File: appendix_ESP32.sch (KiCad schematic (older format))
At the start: 1 part

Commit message: pre Annotation 1
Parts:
- added Q? (x2): 2N3904, digikey-footprints:TO-92-3, symbol dk_Transistors-Bipolar-BJT-Single:2N3904
- added R? (x3): 10k, symbol Device:R
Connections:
- net labels added: DTR_ESP32, ESP32_GPIO0, ESP32_RESET, RTS_ESP32
- wire segments 4 -> 24
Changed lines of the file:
@@
 $Descr A4 11693 8268
 encoding utf-8
-Sheet 3 7
+Sheet 3 6
 Title ""
 Date ""
@@
 EndData
 $EndBitmap
+$Comp
+L dk_Transistors-Bipolar-BJT-Single:2N3904 Q?
+U 1 1 5CBEF82D
+P 9500 2350
+F 0 "Q?" H 9688 2403 60  0000 L CNN
+F 1 "2N3904" H 9688 2297 60  0000 L CNN
+F 2 "digikey-footprints:TO-92-3" H 9700 2550 60  0001 L CNN
+F 3 "https://my.centralsemi.com/get_document.php?cmp=1&mergetype=pd&mergepath=pd&pdf_id=LSSGP072.PDF" H 9700 2650 60  0001 L CNN
+F 4 "2N3904CS-ND" H 9700 2750 60  0001 L CNN "Digi-Key_PN"
+F 5 "2N3904" H 9700 2850 60  0001 L CNN "MPN"
+F 6 "Discrete Semiconductor Products" H 9700 2950 60  0001 L CNN "Category"
+F 7 "Transistors - Bipolar (BJT) - Single" H 9700 3050 60  0001 L CNN "Family"
+F 8 "https://my.centralsemi.com/get_document.php?cmp=1&mergetype=pd&mergepath=pd&pdf_id=LSSGP072.PDF" H 9700 3150 60  0001 L CNN "DK_Datasheet_Link"
+F 9 "/product-detail/en/central-semiconductor-corp/2N3904/2N3904CS-ND/4806876" H 9700 3250 60  0001 L CNN "DK_Detail_Page"
+F 10 "TRANS NPN 40V TO-92" H 9700 3350 60  0001 L CNN "Description"
+F 11 "Central Semiconductor Corp" H 9700 3450 60  0001 L CNN "Manufacturer"
+F 12 "Active" H 9700 3550 60  0001 L CNN "Status"
+	1    9500 2350
+	1    0    0    -1
+$EndComp
+$Comp
+L dk_Transistors-Bipolar-BJT-Single:2N3904 Q?
+U 1 1 5CBF1B4A
+P 9500 3000
+F 0 "Q?" H 9688 2947 60  0000 L CNN
+F 1 "2N3904" H 9688 3053 60  0000 L CNN
+F 2 "digikey-footprints:TO-92-3" H 9700 3200 60  0001 L CNN
+F 3 "https://my.centralsemi.com/get_document.php?cmp=1&mergetype=pd&mergepath=pd&pdf_id=LSSGP072.PDF" H 9700 3300 60  0001 L CNN
+F 4 "2N3904CS-ND" H 9700 3400 60  0001 L CNN "Digi-Key_PN"
+F 5 "2N3904" H 9700 3500 60  0001 L CNN "MPN"
+F 6 "Discrete Semiconductor Products" H 9700 3600 60  0001 L CNN "Category"
+F 7 "Transistors - Bipolar (BJT) - Single" H 9700 3700 60  0001 L CNN "Family"
+F 8 "https://my.centralsemi.com/get_document.php?cmp=1&mergetype=pd&mergepath=pd&pdf_id=LSSGP072.PDF" H 9700 3800 60  0001 L CNN "DK_Datasheet_Link"
+F 9 "/product-detail/en/central-semiconductor-corp/2N3904/2N3904CS-ND/4806876" H 9700 3900 60  0001 L CNN "DK_Detail_Page"
+F 10 "TRANS NPN 40V TO-92" H 9700 4000 60  0001 L CNN "Description"
+F 11 "Central Semiconductor Corp" H 9700 4100 60  0001 L CNN "Manufacturer"
+F 12 "Active" H 9700 4200 60  0001 L CNN "Status"
+	1    9500 3000
+	1    0    0    1
+$EndComp
+$Comp
+L Device:R R?
+U 1 1 5CBF31BB
+P 9000 2350
+F 0 "R?" V 8793 2350 50  0000 C CNN
+F 1 "10k" V 8884 2350 50  0000 C CNN
+F 2 "" V 8930 2350 50  0001 C CNN
+F 3 "~" H 9000 2350 50  0001 C CNN
+	1    9000 2350
+	0    1    1    0
+$EndComp
+$Comp
+L Device:R R?
+U 1 1 5CBF3EA7
+P 9000 3000
+F 0 "R?" V 8793 3000 50  0000 C CNN
+F 1 "10k" V 8884 3000 50  0000 C CNN
+F 2 "" V 8930 3000 50  0001 C CNN
+F 3 "~" H 9000 3000 50  0001 C CNN
+	1    9000 3000
+	0    1    1    0
+$EndComp
+Wire Wire Line
+	9150 3000 9300 3000
+Wire Wire Line
+	9150 2350 9300 2350
+Wire Wire Line
+	8850 3000 8650 3000
+Wire Wire Line
+	9600 2550 9400 2750
+Wire Wire Line
+	8650 2750 9400 2750
+Wire Wire Line
+	8850 2350 8650 2350
+Wire Wire Line
+	8650 2350 8650 2600
+Wire Wire Line
+	8650 2600 9400 2600
+Wire Wire Line
+	9400 2600 9600 2800
+Wire Wire Line
+	8650 2750 8650 3000
+Wire Wire Line
+	8650 2350 8350 2350
+Connection ~ 8650 2350
+Wire Wire Line
+	8650 3000 8350 3000
+Connection ~ 8650 3000
+Text HLabel 8350 3000 0    50   Input ~ 0
+DTR_ESP32
+Text HLabel 8350 2350 0    50   Input ~ 0
+RTS_ESP32
+Wire Wire Line
+	5650 2100 5850 2100
+Text Label 5850 2100 0    50   ~ 0
+ESP32_GPIO0
+Text Label 9650 2100 0    50   ~ 0
+ESP32_GPIO0
+Text Label 9650 3250 0    50   ~ 0
+ESP32_RESET
+Wire Wire Line
+	9650 3250 9600 3250
+Wire Wire Line
+	9600 3250 9600 3200
+Wire Wire Line
+	9600 2150 9600 2100
+Wire Wire Line
+	9600 2100 9650 2100
+Text Label 3550 2100 0    50   ~ 0
+ESP32_RESET
+$Comp
+L Device:R R?
+U 1 1 5CBFAC95
+P 4200 1900
+F 0 "R?" H 4270 1946 50  0000 L CNN
+F 1 "10k" H 4270 1855 50  0000 L CNN
+F 2 "" V 4130 1900 50  0001 C CNN
+F 3 "~" H 4200 1900 50  0001 C CNN
+	1    4200 1900
+	1    0    0    -1
+$EndComp
+$Comp
+L power:+3.3V #PWR?
+U 1 1 5CBFC50E
+P 4200 1750
+F 0 "#PWR?" H 4200 1600 50  0001 C CNN
+F 1 "+3.3V" H 4215 1923 50  0000 C CNN
+F 2 "" H 4200 1750 50  0001 C CNN
+F 3 "" H 4200 1750 50  0001 C CNN
+	1    4200 1750
+	1    0    0    -1
+$EndComp
+Wire Wire Line
+	4450 2100 4200 2100
+Wire Wire Line
+	4200 2050 4200 2100
+Connection ~ 4200 2100
+Wire Wire Line
+	4200 2100 3550 2100
 $EndSCHEMATC

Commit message: 1st annotation, footprints, netlist
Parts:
- R301, R302, R303: renamed from R?; footprint (none) -> Resistors_SMD:R_0805
- gave numbers to parts that had none: 3
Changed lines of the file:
@@
 $EndDescr
 $Comp
-L power:GND #PWR?
+L power:GND #PWR0136
 U 1 1 5CA3C9F2
 P 5050 4850
-F 0 "#PWR?" H 5050 4600 50  0001 C CNN
+F 0 "#PWR0136" H 5050 4600 50  0001 C CNN
 F 1 "GND" H 5055 4677 50  0000 C CNN
 F 2 "" H 5050 4850 50  0001 C CNN
@@
 $EndComp
 $Comp
-L power:+3.3V #PWR?
+L power:+3.3V #PWR0137
 U 1 1 5CA3CA30
 P 5050 1750
-F 0 "#PWR?" H 5050 1600 50  0001 C CNN
+F 0 "#PWR0137" H 5050 1600 50  0001 C CNN
 F 1 "+3.3V" H 5065 1923 50  0000 C CNN
 F 2 "" H 5050 1750 50  0001 C CNN
@@
 D_RX_to_ESP_TX
 $Comp
-L RF_Module:ESP32-WROOM-32 U?
+L RF_Module:ESP32-WROOM-32 U301
 U 1 1 5CA47080
 P 5050 3300
-F 0 "U?" H 5300 4850 50  0000 C CNN
+F 0 "U301" H 5300 4850 50  0000 C CNN
 F 1 "ESP32-WROOM-32" H 5600 4750 50  0000 C CNN
 F 2 "RF_Module:ESP32-WROOM-32" H 5050 1800 50  0001 C CNN
@@
 $EndBitmap
 $Comp
-L dk_Transistors-Bipolar-BJT-Single:2N3904 Q?
+L dk_Transistors-Bipolar-BJT-Single:2N3904 Q301
 U 1 1 5CBEF82D
 P 9500 2350
-F 0 "Q?" H 9688 2403 60  0000 L CNN
+F 0 "Q301" H 9688 2403 60  0000 L CNN
 F 1 "2N3904" H 9688 2297 60  0000 L CNN
 F 2 "digikey-footprints:TO-92-3" H 9700 2550 60  0001 L CNN
@@
 $EndComp
 $Comp
-L dk_Transistors-Bipolar-BJT-Single:2N3904 Q?
+L dk_Transistors-Bipolar-BJT-Single:2N3904 Q302
 U 1 1 5CBF1B4A
 P 9500 3000
-F 0 "Q?" H 9688 2947 60  0000 L CNN
+F 0 "Q302" H 9688 2947 60  0000 L CNN
 F 1 "2N3904" H 9688 3053 60  0000 L CNN
 F 2 "digikey-footprints:TO-92-3" H 9700 3200 60  0001 L CNN
@@
 $EndComp
 $Comp
-L Device:R R?
+L Device:R R302
 U 1 1 5CBF31BB
 P 9000 2350
-F 0 "R?" V 8793 2350 50  0000 C CNN
+F 0 "R302" V 8793 2350 50  0000 C CNN
 F 1 "10k" V 8884 2350 50  0000 C CNN
-F 2 "" V 8930 2350 50  0001 C CNN
+F 2 "Resistors_SMD:R_0805" V 8930 2350 50  0001 C CNN
 F 3 "~" H 9000 2350 50  0001 C CNN
 	1    9000 2350
@@
 $EndComp
 $Comp
-L Device:R R?
+L Device:R R303
 U 1 1 5CBF3EA7
 P 9000 3000
-F 0 "R?" V 8793 3000 50  0000 C CNN
+F 0 "R303" V 8793 3000 50  0000 C CNN
 F 1 "10k" V 8884 3000 50  0000 C CNN
-F 2 "" V 8930 3000 50  0001 C CNN
+F 2 "Resistors_SMD:R_0805" V 8930 3000 50  0001 C CNN
 F 3 "~" H 9000 3000 50  0001 C CNN
 	1    9000 3000
@@
 ESP32_RESET
 $Comp
-L Device:R R?
+L Device:R R301
 U 1 1 5CBFAC95
 P 4200 1900
-F 0 "R?" H 4270 1946 50  0000 L CNN
+F 0 "R301" H 4270 1946 50  0000 L CNN
 F 1 "10k" H 4270 1855 50  0000 L CNN
-F 2 "" V 4130 1900 50  0001 C CNN
+F 2 "Resistors_SMD:R_0805" V 4130 1900 50  0001 C CNN
 F 3 "~" H 4200 1900 50  0001 C CNN
 	1    4200 1900
@@
 $EndComp
 $Comp
-L power:+3.3V #PWR?
+L power:+3.3V #PWR0138
 U 1 1 5CBFC50E
 P 4200 1750
-F 0 "#PWR?" H 4200 1600 50  0001 C CNN
+F 0 "#PWR0138" H 4200 1600 50  0001 C CNN
 F 1 "+3.3V" H 4215 1923 50  0000 C CNN
 F 2 "" H 4200 1750 50  0001 C CNN

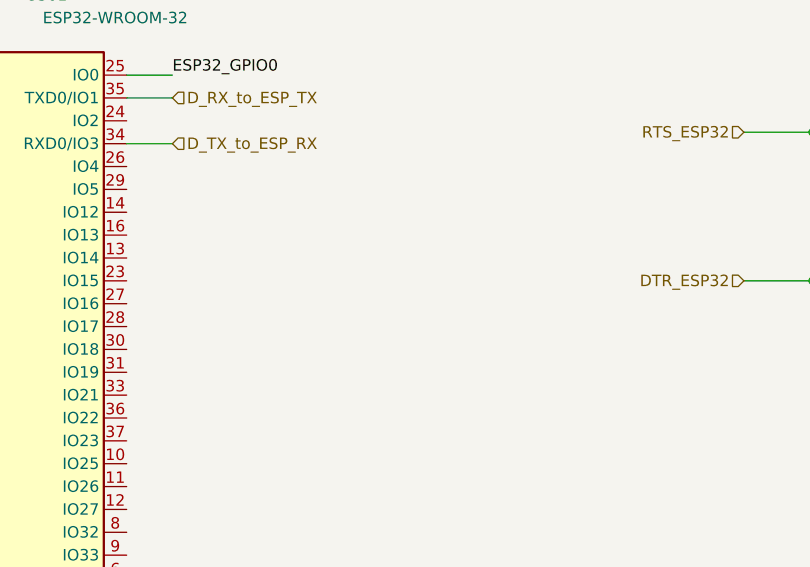
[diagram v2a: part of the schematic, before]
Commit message: started layouting TMC2660
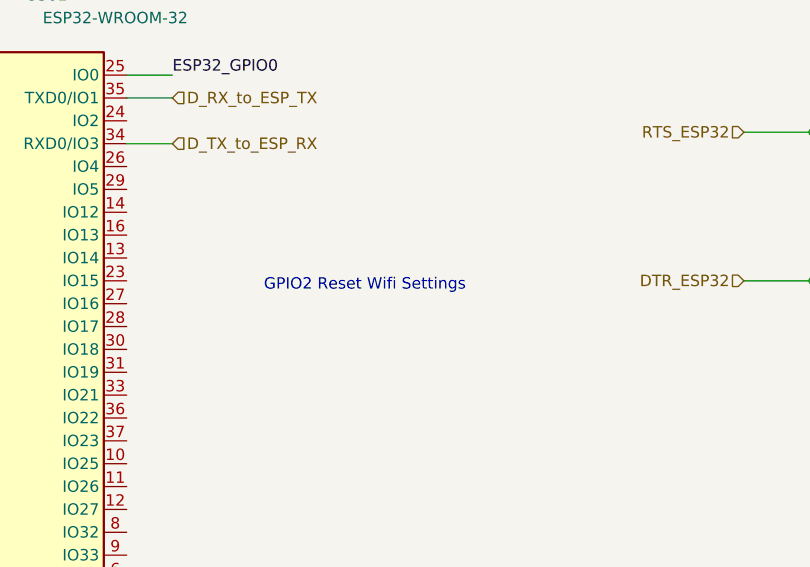
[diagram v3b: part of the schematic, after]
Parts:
- R301, R302, R303: footprint Resistors_SMD:R_0805 -> Resistors_SMD:R_0603
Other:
- note added: "GPIO2 Reset Wifi Settings"
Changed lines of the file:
@@
 F 0 "R302" V 8793 2350 50  0000 C CNN
 F 1 "10k" V 8884 2350 50  0000 C CNN
-F 2 "Resistors_SMD:R_0805" V 8930 2350 50  0001 C CNN
+F 2 "Resistors_SMD:R_0603" V 8930 2350 50  0001 C CNN
 F 3 "~" H 9000 2350 50  0001 C CNN
 	1    9000 2350
@@
 F 0 "R303" V 8793 3000 50  0000 C CNN
 F 1 "10k" V 8884 3000 50  0000 C CNN
-F 2 "Resistors_SMD:R_0805" V 8930 3000 50  0001 C CNN
+F 2 "Resistors_SMD:R_0603" V 8930 3000 50  0001 C CNN
 F 3 "~" H 9000 3000 50  0001 C CNN
 	1    9000 3000
@@
 F 0 "R301" H 4270 1946 50  0000 L CNN
 F 1 "10k" H 4270 1855 50  0000 L CNN
-F 2 "Resistors_SMD:R_0805" V 4130 1900 50  0001 C CNN
+F 2 "Resistors_SMD:R_0603" V 4130 1900 50  0001 C CNN
 F 3 "~" H 4200 1900 50  0001 C CNN
 	1    4200 1900
@@
 Wire Wire Line
 	4200 2100 3550 2100
+Text Notes 6250 3050 0    50   ~ 0
+GPIO2 Reset Wifi Settings
 $EndSCHEMATC

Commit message: Layout: all TMC / Schematic: Oli's comments
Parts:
- added C301, C302: 100n, Capacitors_SMD:C_0603, symbol Device:C
- added R304: 10k, Resistors_SMD:R_0603, symbol Device:R
- added SW301, SW302: SW_Push, Button_Switch_SMD:SW_Push_1P1T_NO_CK_KMR2, symbol Switch:SW_Push
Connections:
- wire segments 24 -> 41
- no-connect marks 0 -> 27
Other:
- note added: "ESP3D Settings Reset"
- note removed: "GPIO2 Reset Wifi Settings"
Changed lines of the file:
@@
 Connection ~ 4200 2100
 Wire Wire Line
-	4200 2100 3550 2100
-Text Notes 6250 3050 0    50   ~ 0
-GPIO2 Reset Wifi Settings
+	4200 2100 3900 2100
+Text Notes 6300 3750 0    50   ~ 0
+ESP3D Settings Reset
+$Comp
+L Switch:SW_Push SW?
+U 1 1 5CD80C30
+P 6500 4050
+AR Path="/5CA3954A/5CD80C30" Ref="SW?"  Part="1"
+AR Path="/5CA395A8/5CD80C30" Ref="SW302"  Part="1"
+F 0 "SW302" V 6650 4250 50  0000 C CNN
+F 1 "SW_Push" V 6300 4300 50  0000 C CNN
+F 2 "Button_Switch_SMD:SW_Push_1P1T_NO_CK_KMR2" H 6500 4250 50  0001 C CNN
+F 3 "~" H 6500 4250 50  0001 C CNN
+	1    6500 4050
+	0    1    -1   0
+$EndComp
+$Comp
+L Device:C C?
+U 1 1 5CD80C36
+P 6200 4050
+AR Path="/5CA3954A/5CD80C36" Ref="C?"  Part="1"
+AR Path="/5CA395A8/5CD80C36" Ref="C302"  Part="1"
+F 0 "C302" H 6000 4150 50  0000 C CNN
+F 1 "100n" H 6350 4150 50  0000 C CNN
+F 2 "Capacitors_SMD:C_0603" H 6238 3900 50  0001 C CNN
+F 3 "~" H 6200 4050 50  0001 C CNN
+	1    6200 4050
+	-1   0    0    -1
+$EndComp
+$Comp
+L power:GND #PWR?
+U 1 1 5CD80C3C
+P 6200 4400
+AR Path="/5CA3954A/5CD80C3C" Ref="#PWR?"  Part="1"
+AR Path="/5CA395A8/5CD80C3C" Ref="#PWR0303"  Part="1"
+F 0 "#PWR0303" H 6200 4150 50  0001 C CNN
+F 1 "GND" H 6205 4227 50  0000 C CNN
+F 2 "" H 6200 4400 50  0001 C CNN
+F 3 "" H 6200 4400 50  0001 C CNN
+	1    6200 4400
+	-1   0    0    -1
+$EndComp
+Wire Wire Line
+	6500 4250 6500 4300
+Wire Wire Line
+	6500 4300 6200 4300
+Wire Wire Line
+	6200 4300 6200 4200
+Wire Wire Line
+	6200 3900 6200 3800
+Wire Wire Line
+	6200 3800 6500 3800
+Wire Wire Line
+	6500 3800 6500 3850
+Wire Wire Line
+	6200 4400 6200 4300
+Connection ~ 6200 4300
+Connection ~ 6200 3800
+$Comp
+L Device:R R?
+U 1 1 5CD80C4C
+P 6200 3600
+AR Path="/5CA3954A/5CD80C4C" Ref="R?"  Part="1"
+AR Path="/5CA395A8/5CD80C4C" Ref="R304"  Part="1"
+F 0 "R304" H 6270 3646 50  0000 L CNN
+F 1 "10k" H 6270 3555 50  0000 L CNN
+F 2 "Resistors_SMD:R_0603" V 6130 3600 50  0001 C CNN
+F 3 "~" H 6200 3600 50  0001 C CNN
+	1    6200 3600
+	-1   0    0    -1
+$EndComp
+Wire Wire Line
+	6200 3800 6200 3750
+$Comp
+L power:+3.3V #PWR?
+U 1 1 5CD80C53
+P 6200 3400
+AR Path="/5CA3954A/5CD80C53" Ref="#PWR?"  Part="1"
+AR Path="/5CA395A8/5CD80C53" Ref="#PWR0302"  Part="1"
+F 0 "#PWR0302" H 6200 3250 50  0001 C CNN
+F 1 "+3.3V" H 6215 3573 50  0000 C CNN
+F 2 "" H 6200 3400 50  0001 C CNN
+F 3 "" H 6200 3400 50  0001 C CNN
+	1    6200 3400
+	-1   0    0    -1
+$EndComp
+Wire Wire Line
+	6200 3400 6200 3450
+NoConn ~ 4450 2300
+NoConn ~ 4450 2400
+$Comp
+L Switch:SW_Push SW?
+U 1 1 5CD83394
+P 3900 2350
+AR Path="/5CA3954A/5CD83394" Ref="SW?"  Part="1"
+AR Path="/5CA395A8/5CD83394" Ref="SW301"  Part="1"
+F 0 "SW301" V 4050 2550 50  0000 C CNN
+F 1 "SW_Push" V 3700 2600 50  0000 C CNN
+F 2 "Button_Switch_SMD:SW_Push_1P1T_NO_CK_KMR2" H 3900 2550 50  0001 C CNN
+F 3 "~" H 3900 2550 50  0001 C CNN
+	1    3900 2350
+	0    -1   -1   0
+$EndComp
+$Comp
+L Device:C C?
+U 1 1 5CD8339E
+P 4200 2350
+AR Path="/5CA3954A/5CD8339E" Ref="C?"  Part="1"
+AR Path="/5CA395A8/5CD8339E" Ref="C301"  Part="1"
+F 0 "C301" H 4000 2450 50  0000 C CNN
+F 1 "100n" H 4050 2200 50  0000 C CNN
+F 2 "Capacitors_SMD:C_0603" H 4238 2200 50  0001 C CNN
+F 3 "~" H 4200 2350 50  0001 C CNN
+	1    4200 2350
+	1    0    0    -1
+$EndComp
+$Comp
+L power:GND #PWR?
+U 1 1 5CD833A8
+P 4200 2700
+AR Path="/5CA3954A/5CD833A8" Ref="#PWR?"  Part="1"
+AR Path="/5CA395A8/5CD833A8" Ref="#PWR0301"  Part="1"
+F 0 "#PWR0301" H 4200 2450 50  0001 C CNN
+F 1 "GND" H 4205 2527 50  0000 C CNN
+F 2 "" H 4200 2700 50  0001 C CNN
+F 3 "" H 4200 2700 50  0001 C CNN
+	1    4200 2700
+	1    0    0    -1
+$EndComp
+Wire Wire Line
+	3900 2550 3900 2600
+Wire Wire Line
+	3900 2600 4200 2600
+Wire Wire Line
+	4200 2600 4200 2500
+Wire Wire Line
+	4200 2200 4200 2100
+Wire Wire Line
+	3900 2100 3900 2150
+Wire Wire Line
+	4200 2700 4200 2600
+Connection ~ 4200 2600
+Connection ~ 3900 2100
+Wire Wire Line
+	3900 2100 3550 2100
+Wire Wire Line
+	6200 3800 5650 3800
+NoConn ~ 4450 3300
+NoConn ~ 4450 3400
+NoConn ~ 4450 3500
+NoConn ~ 4450 3600
+NoConn ~ 4450 3700
+NoConn ~ 4450 3800
+NoConn ~ 5650 4400
+NoConn ~ 5650 4300
+NoConn ~ 5650 4200
+NoConn ~ 5650 4100
+NoConn ~ 5650 4000
+NoConn ~ 5650 3900
+NoConn ~ 5650 3700
+NoConn ~ 5650 3600
+NoConn ~ 5650 3500
+NoConn ~ 5650 3400
+NoConn ~ 5650 3300
+NoConn ~ 5650 3200
+NoConn ~ 5650 3100
+NoConn ~ 5650 3000
+NoConn ~ 5650 2900
+NoConn ~ 5650 2800
+NoConn ~ 5650 2700
+NoConn ~ 5650 2600
+NoConn ~ 5650 2500
 $EndSCHEMATC

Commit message: added footprints, layouted 3v3 Reg
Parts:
- SW301, SW302: footprint Button_Switch_SMD:SW_Push_1P1T_NO_CK_KMR2 -> Button_Switch_SMD:SW_SPST_KMR2

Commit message: added FT2232 by Marco M
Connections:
- net labels added: RX_ESP_to_TX_FTDI, TX_ESP_to_RX_FTDI
- net labels removed: D_RX_to_ESP_TX, D_TX_to_ESP_RX
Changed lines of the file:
@@
 $EndComp
 Text HLabel 5850 2400 2    50   Input ~ 0
-D_TX_to_ESP_RX
+RX_ESP_to_TX_FTDI
 Text HLabel 5850 2200 2    50   Input ~ 0
-D_RX_to_ESP_TX
+TX_ESP_to_RX_FTDI
 $Comp
 L RF_Module:ESP32-WROOM-32 U301
